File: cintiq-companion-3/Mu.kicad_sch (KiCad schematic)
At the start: 12 parts, among them J1 Conn_01x03_Pin

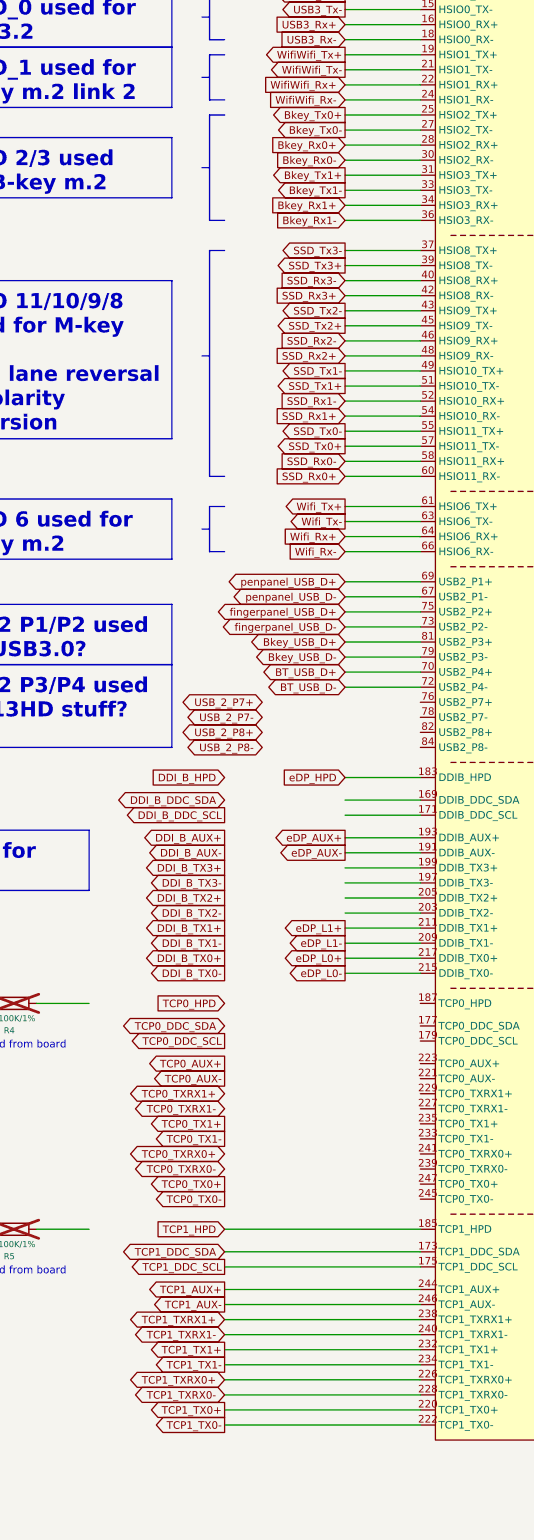
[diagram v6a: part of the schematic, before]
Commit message: flipped b-key lane order and added usb-c ports
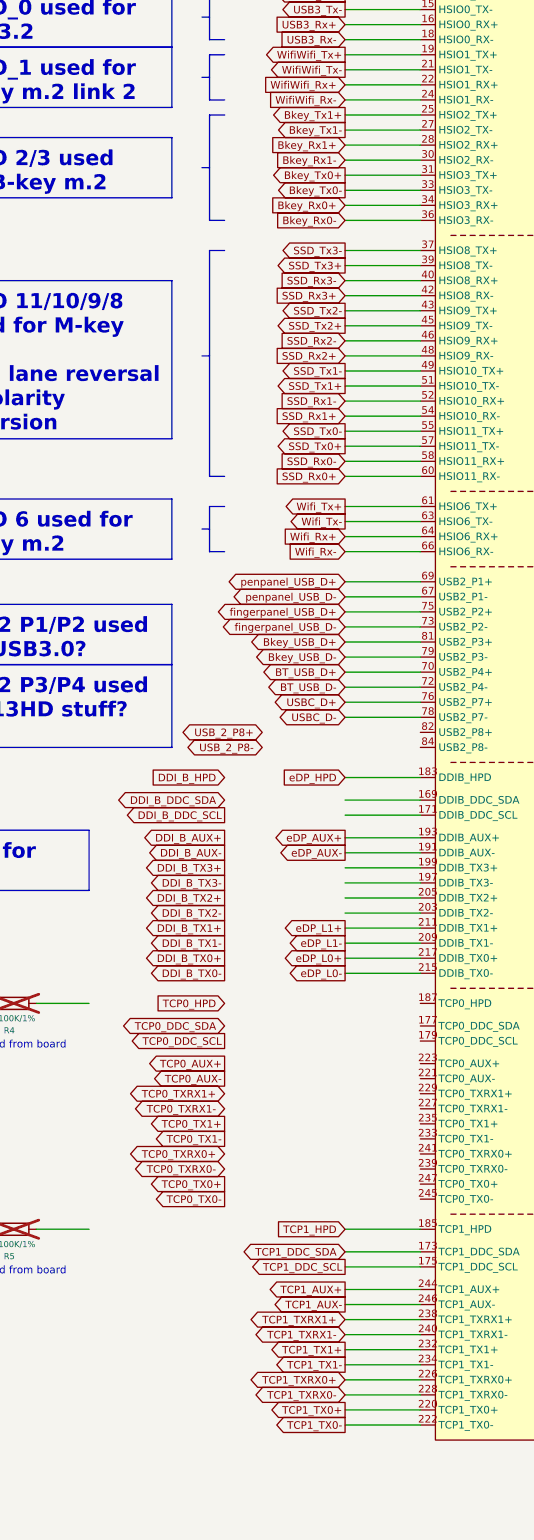
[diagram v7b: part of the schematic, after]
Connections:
- net Bkey_Rx0+: now also A1.34 (HSIO3_RX+); no longer A1.28 (HSIO2_RX+)
- net Bkey_Rx0-: now also A1.36 (HSIO3_RX-); no longer A1.30 (HSIO2_RX-)
- net Bkey_Rx1+: now also A1.28 (HSIO2_RX+); no longer A1.34 (HSIO3_RX+)
- net Bkey_Rx1-: now also A1.30 (HSIO2_RX-); no longer A1.36 (HSIO3_RX-)
- net Bkey_Tx0+: now also A1.31 (HSIO3_TX+); no longer A1.25 (HSIO2_TX+)
- net Bkey_Tx0-: now also A1.33 (HSIO3_TX-); no longer A1.27 (HSIO2_TX-)
- net Bkey_Tx1+: now also A1.25 (HSIO2_TX+); no longer A1.31 (HSIO3_TX+)
- net Bkey_Tx1-: now also A1.27 (HSIO2_TX-); no longer A1.33 (HSIO3_TX-)
- net USBC_D+: now reaches A1.76 (USB2_P7+)
- net USBC_D-: now reaches A1.78 (USB2_P7-)
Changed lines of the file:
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@@
 	(wire
 		(pts
-			(xy 313.69 298.45) (xy 346.71 298.45)
+			(xy 334.01 298.45) (xy 346.71 298.45)
 		)
 		(stroke
@@
 	(wire
 		(pts
-			(xy 313.69 318.77) (xy 346.71 318.77)
+			(xy 334.01 318.77) (xy 346.71 318.77)
 		)
 		(stroke
@@
 	(wire
 		(pts
-			(xy 313.69 304.8) (xy 346.71 304.8)
+			(xy 334.01 304.8) (xy 346.71 304.8)
 		)
 		(stroke
@@
 	(wire
 		(pts
-			(xy 313.69 331.47) (xy 346.71 331.47)
+			(xy 334.01 331.47) (xy 346.71 331.47)
 		)
 		(stroke
@@
 	(wire
 		(pts
-			(xy 313.69 321.31) (xy 346.71 321.31)
+			(xy 334.01 321.31) (xy 346.71 321.31)
 		)
 		(stroke
@@
 	(wire
 		(pts
-			(xy 313.69 308.61) (xy 346.71 308.61)
+			(xy 334.01 308.61) (xy 346.71 308.61)
 		)
 		(stroke
@@
 	(wire
 		(pts
-			(xy 313.69 302.26) (xy 346.71 302.26)
+			(xy 334.01 302.26) (xy 346.71 302.26)
 		)
 		(stroke
@@
 	(wire
 		(pts
-			(xy 313.69 313.69) (xy 346.71 313.69)
+			(xy 334.01 313.69) (xy 346.71 313.69)
 		)
 		(stroke
@@
 	(wire
 		(pts
-			(xy 313.69 311.15) (xy 346.71 311.15)
+			(xy 334.01 311.15) (xy 346.71 311.15)
 		)
 		(stroke
@@
 	(wire
 		(pts
-			(xy 313.69 326.39) (xy 346.71 326.39)
+			(xy 334.01 326.39) (xy 346.71 326.39)
 		)
 		(stroke
@@
 	(wire
 		(pts
+			(xy 334.01 212.09) (xy 346.71 212.09)
+		)
+		(stroke
+			(width 0)
+			(type default)
+		)
+	)
+	(wire
+		(pts
 			(xy 400.05 55.88) (xy 408.94 55.88)
 		)
@@
 	(wire
 		(pts
-			(xy 313.69 316.23) (xy 346.71 316.23)
+			(xy 334.01 316.23) (xy 346.71 316.23)
 		)
 		(stroke
@@
 	(wire
 		(pts
+			(xy 334.01 209.55) (xy 346.71 209.55)
+		)
+		(stroke
+			(width 0)
+			(type default)
+		)
+	)
+	(wire
+		(pts
 			(xy 334.01 196.85) (xy 346.71 196.85)
 		)
@@
 	(wire
 		(pts
-			(xy 313.69 323.85) (xy 346.71 323.85)
+			(xy 334.01 323.85) (xy 346.71 323.85)
 		)
 		(stroke
@@
 	(wire
 		(pts
-			(xy 313.69 328.93) (xy 346.71 328.93)
+			(xy 334.01 328.93) (xy 346.71 328.93)
 		)
 		(stroke
@@
 	(global_label "Bkey_Tx1+"
 		(shape output)
-		(at 334.01 120.65 180)
+		(at 334.01 110.49 180)
 		(fields_autoplaced yes)
 		(effects
@@
 		)
 		(property "Intersheetrefs" "${INTERSHEET_REFS}"
-			(at 320.9253 120.65 0)
+			(at 320.9253 110.49 0)
 			(effects
 				(font
@@
 	(global_label "TCP1_TX1-"
 		(shape output)
-		(at 313.69 321.31 180)
+		(at 334.01 321.31 180)
 		(fields_autoplaced yes)
 		(effects
@@
 		)
 		(property "Intersheetrefs" "${INTERSHEET_REFS}"
-			(at 313.69 321.31 0)
+			(at 334.01 321.31 0)
 			(effects
 				(font
@@
 	(global_label "TCP1_TXRX0+"
 		(shape bidirectional)
-		(at 313.69 323.85 180)
+		(at 334.01 323.85 180)
 		(fields_autoplaced yes)
 		(effects
@@
 		)
 		(property "Intersheetrefs" "${INTERSHEET_REFS}"
-			(at 313.69 323.85 0)
+			(at 334.01 323.85 0)
 			(effects
 				(font
@@
 	(global_label "TCP1_DDC_SDA"
 		(shape bidirectional)
-		(at 313.69 302.26 180)
+		(at 334.01 302.26 180)
 		(fields_autoplaced yes)
 		(effects
@@
 		)
 		(property "Intersheetrefs" "${INTERSHEET_REFS}"
-			(at 313.69 302.26 0)
+			(at 334.01 302.26 0)
 			(effects
 				(font
@@
 	(global_label "TCP1_TXRX1+"
 		(shape bidirectional)
-		(at 313.69 313.69 180)
+		(at 334.01 313.69 180)
 		(fields_autoplaced yes)
 		(effects
@@
 		)
 		(property "Intersheetrefs" "${INTERSHEET_REFS}"
-			(at 313.69 313.69 0)
+			(at 334.01 313.69 0)
 			(effects
 				(font
@@
 	(global_label "TCP1_AUX+"
 		(shape output)
-		(at 313.69 308.61 180)
+		(at 334.01 308.61 180)
 		(fields_autoplaced yes)
 		(effects
@@
 		)
 		(property "Intersheetrefs" "${INTERSHEET_REFS}"
-			(at 313.69 308.61 0)
+			(at 334.01 308.61 0)
 			(effects
 				(font
@@
 	(global_label "TCP1_AUX-"
 		(shape output)
-		(at 313.69 311.15 180)
+		(at 334.01 311.15 180)
 		(fields_autoplaced yes)
 		(effects
@@
 		)
 		(property "Intersheetrefs" "${INTERSHEET_REFS}"
-			(at 313.69 311.15 0)
+			(at 334.01 311.15 0)
 			(effects
 				(font
@@
 	(global_label "TCP1_HPD"
 		(shape input)
-		(at 313.69 298.45 180)
+		(at 334.01 298.45 180)
 		(fields_autoplaced yes)
 		(effects
@@
 		)
 		(property "Intersheetrefs" "${INTERSHEET_REFS}"
-			(at 313.69 298.45 0)
+			(at 334.01 298.45 0)
 			(effects
 				(font
@@
 		)
 	)
-	(global_label "USB_2_P7-"
+	(global_label "USBC_D-"
 		(shape bidirectional)
-		(at 320.04 212.09 180)
+		(at 334.01 212.09 180)
 		(fields_autoplaced yes)
 		(effects
@@
 		)
 		(property "Intersheetrefs" "${INTERSHEET_REFS}"
-			(at 320.04 212.09 0)
+			(at 321.0235 212.09 0)
 			(effects
 				(font
 					(size 1.27 1.27)
 				)
+				(justify right)
 				(hide yes)
 			)
@@
 	(global_label "TCP1_TXRX1-"
 		(shape bidirectional)
-		(at 313.69 316.23 180)
+		(at 334.01 316.23 180)
 		(fields_autoplaced yes)
 		(effects
@@
 		)
 		(property "Intersheetrefs" "${INTERSHEET_REFS}"
-			(at 313.69 316.23 0)
+			(at 334.01 316.23 0)
 			(effects
 				(font
@@
 	(global_label "TCP1_TX0-"
 		(shape output)
-		(at 313.69 331.47 180)
+		(at 334.01 331.47 180)
 		(fields_autoplaced yes)
 		(effects
@@
 		)
 		(property "Intersheetrefs" "${INTERSHEET_REFS}"
-			(at 313.69 331.47 0)
+			(at 334.01 331.47 0)
 			(effects
 				(font
@@
 	(global_label "Bkey_Tx0+"
 		(shape output)
-		(at 334.01 110.49 180)
+		(at 334.01 120.65 180)
 		(fields_autoplaced yes)
 		(effects
@@
 		)
 		(property "Intersheetrefs" "${INTERSHEET_REFS}"
-			(at 320.9253 110.49 0)
+			(at 320.9253 120.65 0)
 			(effects
 				(font
@@
 	(global_label "TCP1_TXRX0-"
 		(shape bidirectional)
-		(at 313.69 326.39 180)
+		(at 334.01 326.39 180)
 		(fields_autoplaced yes)
 		(effects
@@
 		)
 		(property "Intersheetrefs" "${INTERSHEET_REFS}"
-			(at 313.69 326.39 0)
+			(at 334.01 326.39 0)
 			(effects
 				(font
@@
 	(global_label "Bkey_Tx0-"
 		(shape output)
-		(at 334.01 113.03 180)
+		(at 334.01 123.19 180)
 		(fields_autoplaced yes)
 		(effects
@@
 		)
 		(property "Intersheetrefs" "${INTERSHEET_REFS}"
-			(at 320.9253 113.03 0)
+			(at 320.9253 123.19 0)
 			(effects
 				(font
@@
 	(global_label "Bkey_Rx1-"
 		(shape input)
-		(at 334.01 128.27 180)
+		(at 334.01 118.11 180)
 		(fields_autoplaced yes)
 		(effects
@@
 		)
 		(property "Intersheetrefs" "${INTERSHEET_REFS}"
-			(at 320.6229 128.27 0)
+			(at 320.6229 118.11 0)
 			(effects
 				(font
@@
 	(global_label "Bkey_Tx1-"
 		(shape output)
-		(at 334.01 123.19 180)
+		(at 334.01 113.03 180)
 		(fields_autoplaced yes)
 		(effects
@@
 		)
 		(property "Intersheetrefs" "${INTERSHEET_REFS}"
-			(at 320.9253 123.19 0)
+			(at 320.9253 113.03 0)
 			(effects
 				(font
@@
 	(global_label "TCP1_DDC_SCL"
 		(shape output)
-		(at 313.69 304.8 180)
+		(at 334.01 304.8 180)
 		(fields_autoplaced yes)
 		(effects
@@
 		)
 		(property "Intersheetrefs" "${INTERSHEET_REFS}"
-			(at 313.69 304.8 0)
+			(at 334.01 304.8 0)
 			(effects
 				(font
@@
 	(global_label "Bkey_Rx0-"
 		(shape input)
-		(at 334.01 118.11 180)
+		(at 334.01 128.27 180)
 		(fields_autoplaced yes)
 		(effects
@@
 		)
 		(property "Intersheetrefs" "${INTERSHEET_REFS}"
-			(at 320.6229 118.11 0)
+			(at 320.6229 128.27 0)
 			(effects
 				(font
@@
 	(global_label "Bkey_Rx0+"
 		(shape input)
-		(at 334.01 115.57 180)
+		(at 334.01 125.73 180)
 		(fields_autoplaced yes)
 		(effects
@@
 		)
 		(property "Intersheetrefs" "${INTERSHEET_REFS}"
-			(at 320.6229 115.57 0)
+			(at 320.6229 125.73 0)
 			(effects
 				(font
@@
 	(global_label "TCP1_TX1+"
 		(shape output)
-		(at 313.69 318.77 180)
+		(at 334.01 318.77 180)
 		(fields_autoplaced yes)
 		(effects
@@
 		)
 		(property "Intersheetrefs" "${INTERSHEET_REFS}"
-			(at 313.69 318.77 0)
+			(at 334.01 318.77 0)
 			(effects
 				(font
@@
 	(global_label "TCP1_TX0+"
 		(shape output)
-		(at 313.69 328.93 180)
+		(at 334.01 328.93 180)
 		(fields_autoplaced yes)
 		(effects
@@
 		)
 		(property "Intersheetrefs" "${INTERSHEET_REFS}"
-			(at 313.69 328.93 0)
+			(at 334.01 328.93 0)
 			(effects
 				(font
@@
 	(global_label "Bkey_Rx1+"
 		(shape input)
-		(at 334.01 125.73 180)
+		(at 334.01 115.57 180)
 		(fields_autoplaced yes)
 		(effects
@@
 		)
 		(property "Intersheetrefs" "${INTERSHEET_REFS}"
-			(at 320.6229 125.73 0)
+			(at 320.6229 115.57 0)
 			(effects
 				(font
@@
 		)
 	)
-	(global_label "USB_2_P7+"
+	(global_label "USBC_D+"
 		(shape bidirectional)
-		(at 320.04 209.55 180)
+		(at 334.01 209.55 180)
 		(fields_autoplaced yes)
 		(effects
@@
 		)
 		(property "Intersheetrefs" "${INTERSHEET_REFS}"
-			(at 320.04 209.55 0)
+			(at 321.0235 209.55 0)
 			(effects
 				(font
 					(size 1.27 1.27)
 				)
+				(justify right)
 				(hide yes)
 			)

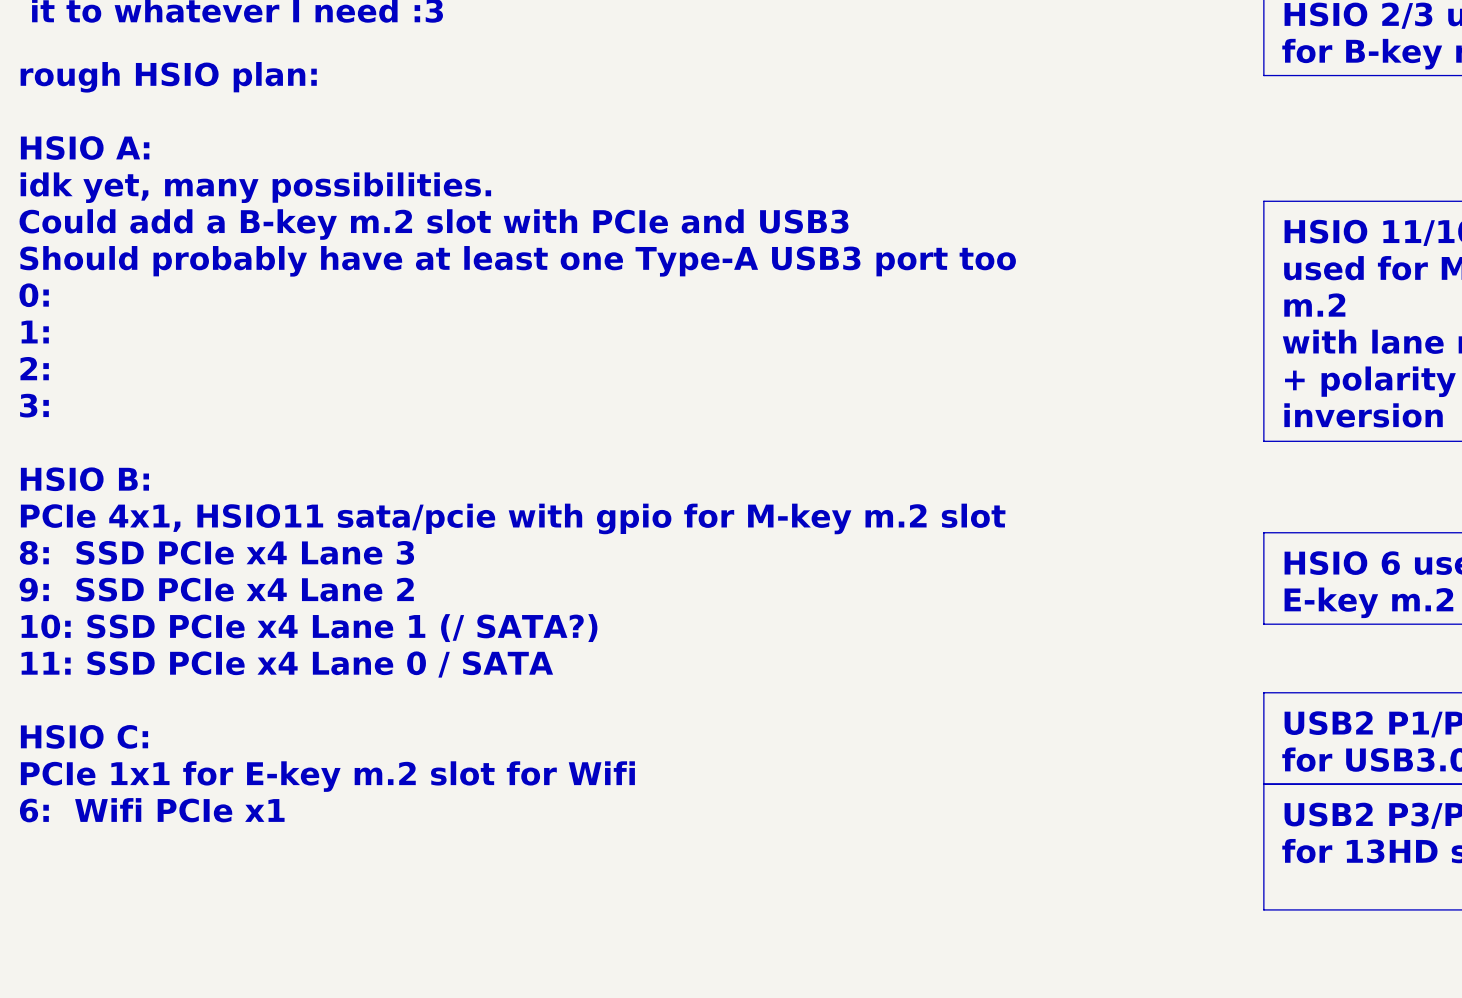
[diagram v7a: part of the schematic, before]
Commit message: updated hsio description
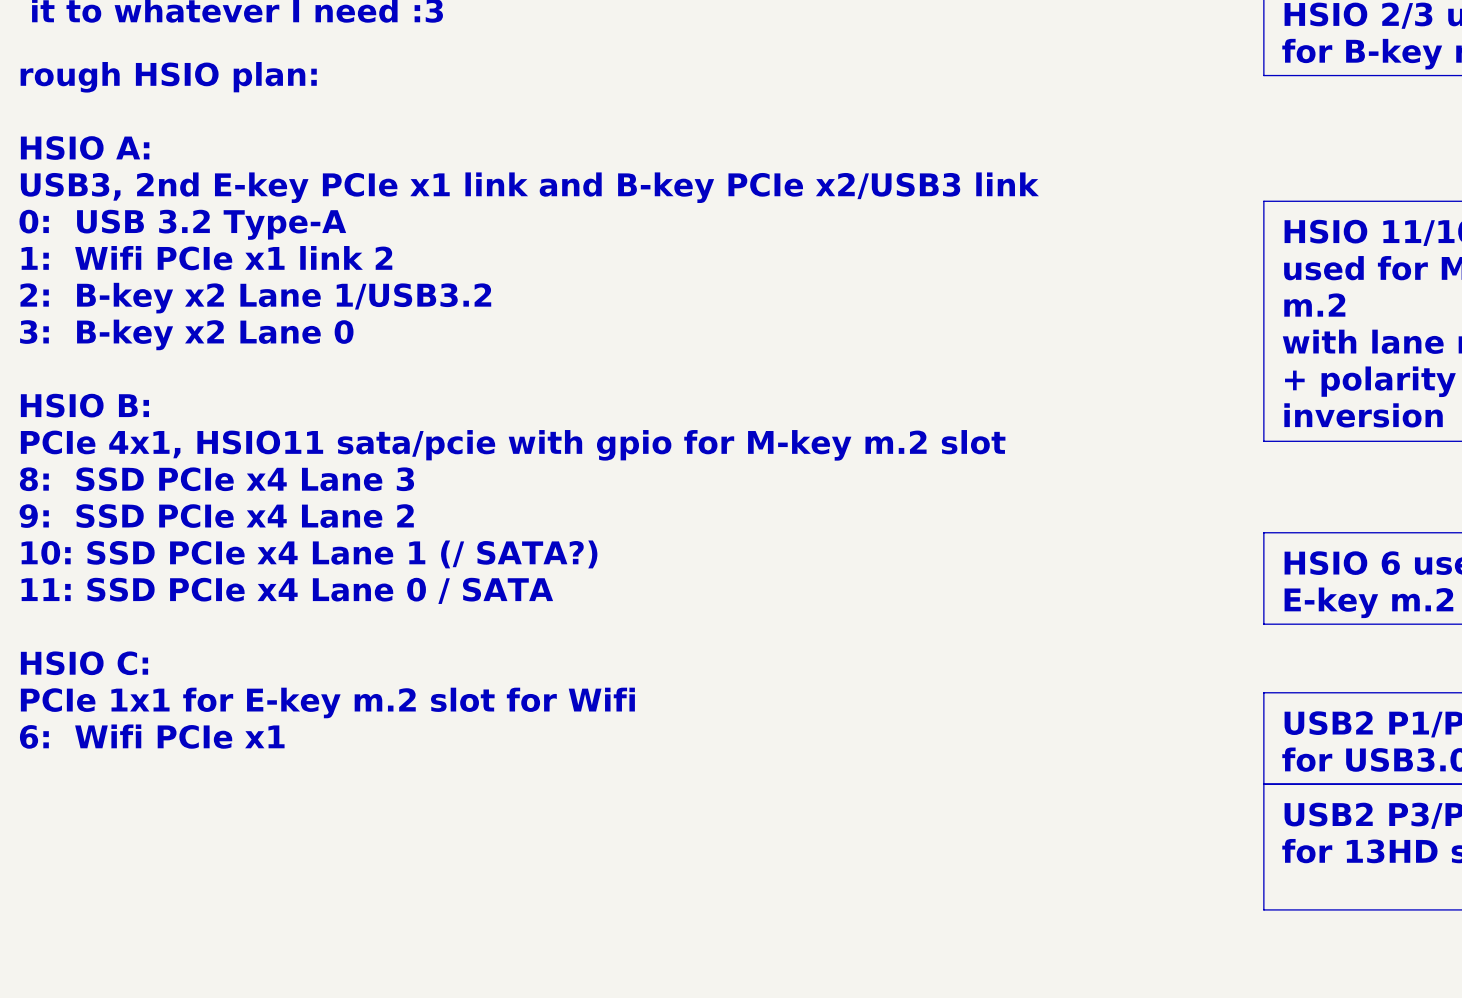
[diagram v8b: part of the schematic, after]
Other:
- note added: "rough HSIO plan: HSIO A: USB3, 2nd E-key PCIe x1 link and B-key PCIe x2/USB3 link 0: USB 3.2 Type-A 1: Wifi PCIe x1 link 2 2: B-key x2 Lane 1/USB3.2 3: B-key x2 Lane 0 HSIO B: PCIe 4x1, HSIO11 sata/pcie with gpio for M-key m.2 slot 8: SSD PCIe x4 Lane 3 9: SSD PCIe x4 Lane 2 10: SSD PCIe x4 Lane 1 (/ SATA?) 11: SSD PCIe x4 Lane 0 / SATA HSIO C: PCIe 1x1 for E-key m.2 slot for Wifi 6: Wifi PCIe x1"
- note removed: "rough HSIO plan: HSIO A: idk yet, many possibilities. Could add a B-key m.2 slot with PCIe and USB3 Should probably have at least one Type-A USB3 port too 0: 1: 2: 3: HSIO B: PCIe 4x1, HSIO11 sata/pcie with gpio for M-key m.2 slot 8: SSD PCIe x4 Lane 3 9: SSD PCIe x4 Lane 2 10: SSD PCIe x4 Lane 1 (/ SATA?) 11: SSD PCIe x4 Lane 0 / SATA HSIO C: PCIe 1x1 for E-key m.2 slot for Wifi 6: Wifi PCIe x1"
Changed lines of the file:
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@@
 		)
 	)
-	(text "rough HSIO plan:\n\nHSIO A:\nidk yet, many possibilities.\nCould add a B-key m.2 slot with PCIe and USB3\nShould probably have at least one Type-A USB3 port too\n0:  \n1:  \n2:  \n3:  \n\nHSIO B:\nPCIe 4x1, HSIO11 sata/pcie with gpio for M-key m.2 slot\n8:  SSD PCIe x4 Lane 3\n9:  SSD PCIe x4 Lane 2\n10: SSD PCIe x4 Lane 1 (/ SATA?)\n11: SSD PCIe x4 Lane 0 / SATA\n\nHSIO C:\nPCIe 1x1 for E-key m.2 slot for Wifi\n6:  Wifi PCIe x1 "
+	(text "rough HSIO plan:\n\nHSIO A:\nUSB3, 2nd E-key PCIe x1 link and B-key PCIe x2/USB3 link\n0:  USB 3.2 Type-A\n1:  Wifi PCIe x1 link 2\n2:  B-key x2 Lane 1/USB3.2\n3:  B-key x2 Lane 0\n\nHSIO B:\nPCIe 4x1, HSIO11 sata/pcie with gpio for M-key m.2 slot\n8:  SSD PCIe x4 Lane 3\n9:  SSD PCIe x4 Lane 2\n10: SSD PCIe x4 Lane 1 (/ SATA?)\n11: SSD PCIe x4 Lane 0 / SATA\n\nHSIO C:\nPCIe 1x1 for E-key m.2 slot for Wifi\n6:  Wifi PCIe x1 "
 		(exclude_from_sim no)
 		(at 127 123.19 0)
